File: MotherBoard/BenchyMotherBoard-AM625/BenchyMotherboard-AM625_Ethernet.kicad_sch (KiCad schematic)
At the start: 59 parts, among them U1 AM6254ATCGGAALW, U10 KSZ9021RN, U11 RJMG212S21130ER, U12 KSZ9021RN, U33 74LVC1G08GW,125, U74 TC7PZ17FU,LJ(CT, U75 TC7PZ17FU,LJ(CT

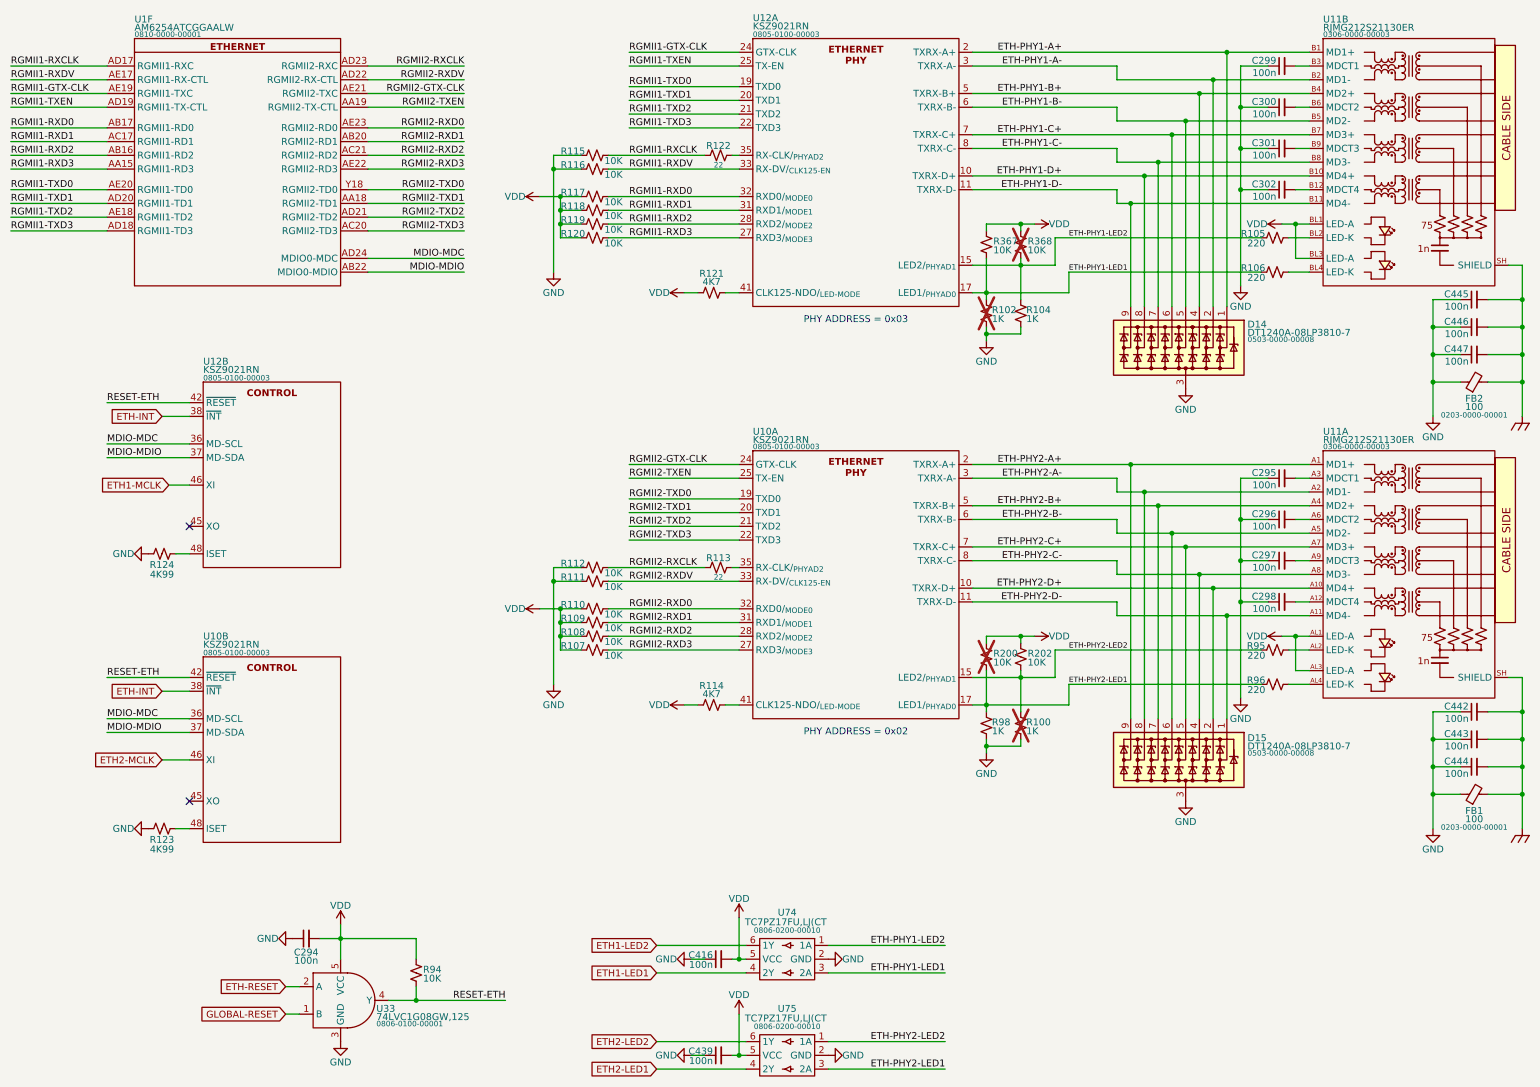
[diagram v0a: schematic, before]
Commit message: Schematic capture mostly complete. Starting PCB layout
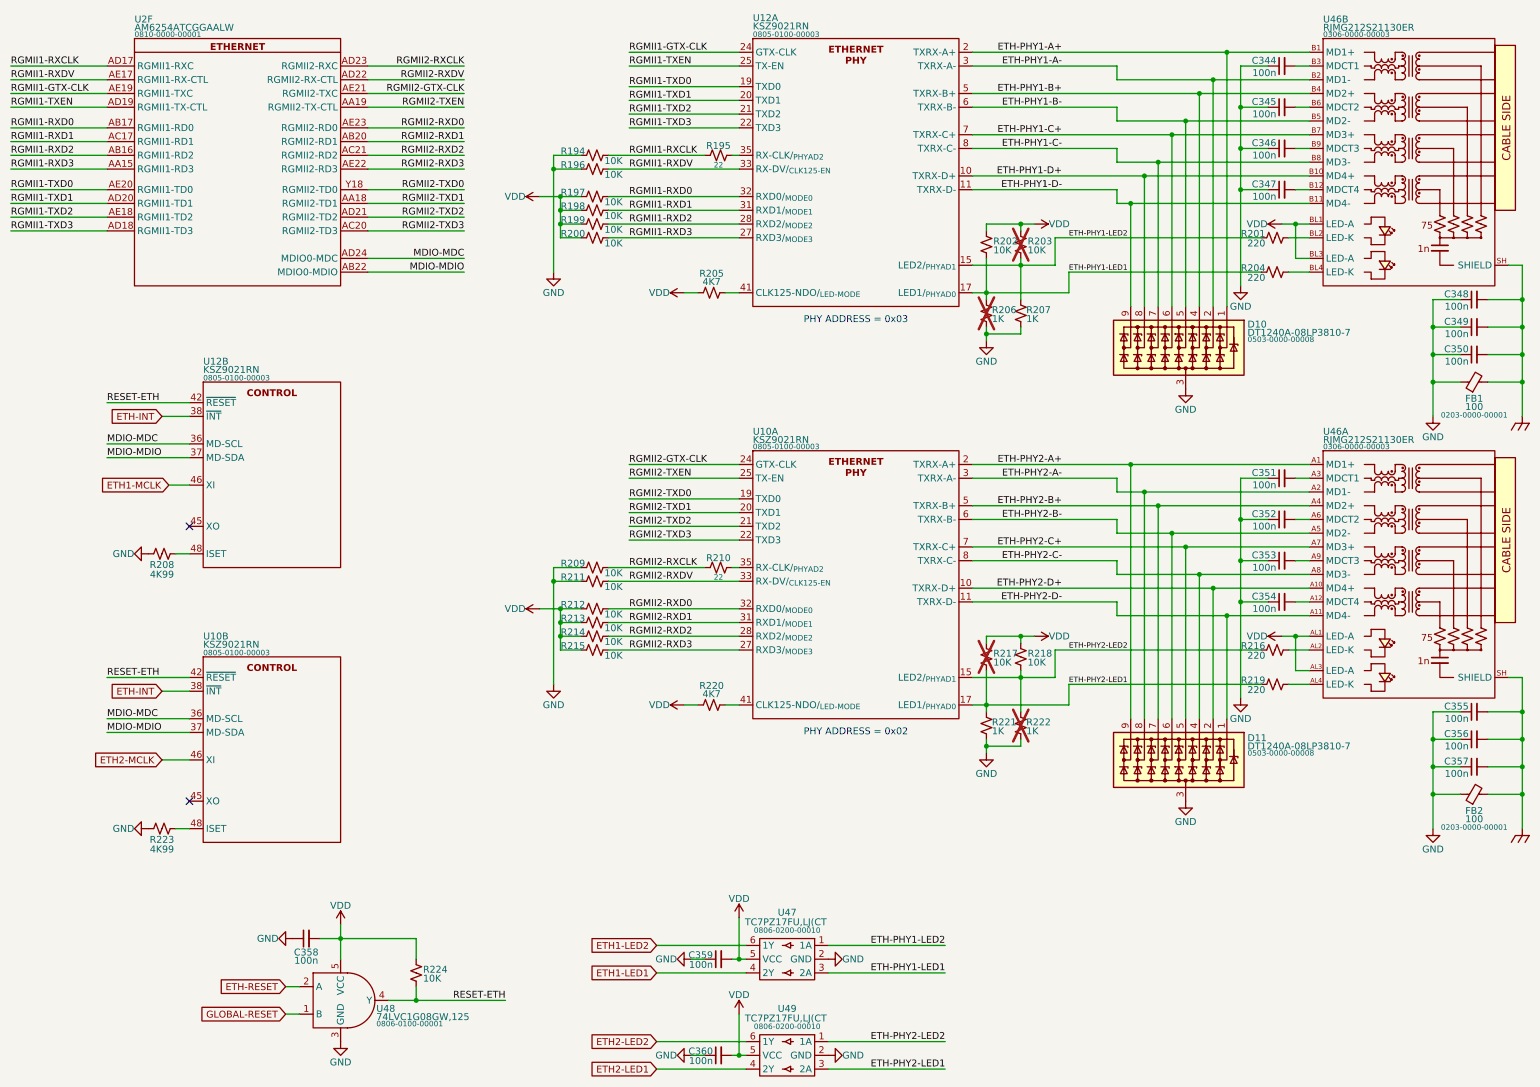
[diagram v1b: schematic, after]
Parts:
- renumbered C299 to C344, C300 to C345, C301 to C346, C302 to C347, C445 to C348, C446 to C349, C447 to C350, C295 to C351, C296 to C352, C297 to C353, C298 to C354, C442 to C355, C443 to C356, C444 to C357, C294 to C358, C416 to C359, C439 to C360, D14 to D10, D15 to D11, FB2 to FB1, FB1 to FB2, R115 to R194, R122 to R195, R116 to R196, R117 to R197, R118 to R198, R119 to R199, R120 to R200, R105 to R201, R367 to R202, R368 to R203, R106 to R204, R121 to R205, R102 to R206, R104 to R207, R124 to R208, R112 to R209, R113 to R210, R111 to R211, R110 to R212, R109 to R213, R108 to R214, R107 to R215, R95 to R216, R200 to R217, R202 to R218, R96 to R219, R114 to R220, R98 to R221, R100 to R222, R123 to R223, R94 to R224, U1 to U2, U11 to U46, U74 to U47, U33 to U48, U75 to U49
